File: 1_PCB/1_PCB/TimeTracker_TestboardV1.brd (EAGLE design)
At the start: 102.5 x 81.3 mm, 18 parts, among them IC1 7805DT, IC2 7805DT, J1 2908-05WB-MG, U1 WS2812B, U2 WS2812B, U3 WS2812B, U4 WS2812B

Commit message: fucvk u raj
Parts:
- added JP5: (no value), jumper:JP1
- added LED_12V1: (no value), led:SML0805
- added R3: 560, rcl:R0805
- added RESET1: (no value), switch-omron:B3F-10XX
- moved J1 4.02 mm to (7.62, 7.62)
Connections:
- new net GND1: RESET1.1, RESET1.2, U$1.RST
- new net N$12: JP5.2, U$1.RAW
- new net N$35: LED_12V1.A, R3.1
- net 5V: now also JP5.1
- net GND: now also LED_12V1.C, RESET1.3, RESET1.4, U$1.GND, U$1.GND1
- net N$1: now also R3.2
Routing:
- net N$13: track 0.00 -> 100.1 mm
- net N$12: track 0.00 -> 2.54 mm
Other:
- board size 102.5 x 81.3 mm -> 102.5 x 80 mm
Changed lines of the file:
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@@
 <board>
 <plain>
-<wire x1="-2.54" y1="-1.27" x2="100" y2="0" width="0" layer="20"/>
-<wire x1="100" y1="0" x2="100" y2="80" width="0" layer="20"/>
-<wire x1="100" y1="80" x2="-2.54" y2="78.73" width="0" layer="20"/>
+<wire x1="-2.54" y1="-1.27" x2="38.1" y2="-1.27" width="0" layer="20"/>
+<wire x1="38.1" y1="-1.27" x2="44.45" y2="5.08" width="0" layer="20"/>
+<wire x1="44.45" y1="5.08" x2="68.58" y2="5.08" width="0" layer="20"/>
+<wire x1="68.58" y1="5.08" x2="74.93" y2="-1.27" width="0" layer="20"/>
+<wire x1="74.93" y1="-1.27" x2="95.25" y2="-1.27" width="0" layer="20"/>
+<wire x1="95.25" y1="-1.27" x2="100" y2="2.635525" width="0" layer="20"/>
+<wire x1="100" y1="2.635525" x2="100" y2="76.19" width="0" layer="20"/>
+<wire x1="100" y1="76.19" x2="97.726525" y2="78.772415625" width="0" layer="20"/>
+<wire x1="97.726525" y1="78.772415625" x2="-2.54" y2="78.73" width="0" layer="20"/>
 <wire x1="-2.54" y1="78.73" x2="-2.54" y2="-1.27" width="0" layer="20"/>
 </plain>
@@
 </autorouter>
 <elements>
-<element name="J1" library="2908-05WB-MG" package="3M_2908-05WB-MG" value="2908-05WB-MG" x="11.43" y="8.89" smashed="yes" rot="R180">
-<attribute name="AVAILABILITY" value="Unavailable" x="-11.43" y="57.15" size="1.778" layer="27" rot="R180" display="off"/>
-<attribute name="DESCRIPTION" value=" 2908-05WB-MG Conn Micro S D Card HDR 8 POS 1.1mm So lder RA SMD T/R 0.5A RoHS " x="-11.43" y="57.15" size="1.778" layer="27" rot="R180" display="off"/>
-<attribute name="MF" value="3M" x="-11.43" y="57.15" size="1.778" layer="27" rot="R180" display="off"/>
-<attribute name="MP" value="2908-05WB-MG" x="-11.43" y="57.15" size="1.778" layer="27" rot="R180" display="off"/>
-<attribute name="NAME" x="19.07195" y="15.791759375" size="1.27031875" layer="25" rot="R270"/>
-<attribute name="PACKAGE" value="None" x="-11.43" y="57.15" size="1.778" layer="27" rot="R180" display="off"/>
-<attribute name="PRICE" value="None" x="-11.43" y="57.15" size="1.778" layer="27" rot="R180" display="off"/>
-<attribute name="VALUE" x="2.768609375" y="15.89111875" size="1.2702" layer="27" rot="R270"/>
+<element name="J1" library="2908-05WB-MG" package="3M_2908-05WB-MG" value="2908-05WB-MG" x="7.62" y="7.62" smashed="yes" rot="R180">
+<attribute name="AVAILABILITY" value="Unavailable" x="-15.24" y="55.88" size="1.778" layer="27" rot="R180" display="off"/>
+<attribute name="DESCRIPTION" value=" 2908-05WB-MG Conn Micro S D Card HDR 8 POS 1.1mm So lder RA SMD T/R 0.5A RoHS " x="-15.24" y="55.88" size="1.778" layer="27" rot="R180" display="off"/>
+<attribute name="MF" value="3M" x="-15.24" y="55.88" size="1.778" layer="27" rot="R180" display="off"/>
+<attribute name="MP" value="2908-05WB-MG" x="-15.24" y="55.88" size="1.778" layer="27" rot="R180" display="off"/>
+<attribute name="NAME" x="15.26195" y="14.521759375" size="1.27031875" layer="25" rot="R270"/>
+<attribute name="PACKAGE" value="None" x="-15.24" y="55.88" size="1.778" layer="27" rot="R180" display="off"/>
+<attribute name="PRICE" value="None" x="-15.24" y="55.88" size="1.778" layer="27" rot="R180" display="off"/>
+<attribute name="VALUE" x="-1.041390625" y="14.62111875" size="1.2702" layer="27" rot="R270"/>
 </element>
 <element name="U$1" library="NanoUSW" package="NANO" value="NANO" x="49.53" y="30.48" smashed="yes"/>
@@
 <attribute name="NAME" x="-11.43" y="-4.445" size="1.27" layer="25" ratio="10"/>
 <attribute name="VALUE" x="-11.43" y="-12.065" size="1.27" layer="27"/>
+</element>
+<element name="RESET1" library="switch-omron" library_urn="urn:adsk.eagle:library:377" package="B3F-10XX" package3d_urn="urn:adsk.eagle:package:27496/1" value="" x="31.369" y="24.384" smashed="yes">
+<attribute name="MF" value="" x="21.209" y="37.084" size="1.778" layer="27" display="off"/>
+<attribute name="MPN" value="B3F-1000" x="21.209" y="37.084" size="1.778" layer="27" display="off"/>
+<attribute name="NAME" x="28.321" y="28.067" size="1.27" layer="25" ratio="10"/>
+<attribute name="OC_FARNELL" value="176432" x="21.209" y="37.084" size="1.778" layer="27" display="off"/>
+<attribute name="OC_NEWARK" value="36M3542" x="21.209" y="37.084" size="1.778" layer="27" display="off"/>
+<attribute name="VALUE" x="28.321" y="19.304" size="1.27" layer="27" ratio="10"/>
+</element>
+<element name="R3" library="rcl" library_urn="urn:adsk.eagle:library:334" package="R0805" package3d_urn="urn:adsk.eagle:package:23553/2" value="560" x="1.27" y="66.04" smashed="yes" rot="R90">
+<attribute name="NAME" x="0" y="65.405" size="1.27" layer="25" rot="R90"/>
+<attribute name="SPICEPREFIX" value="R" x="1.27" y="66.04" size="1.778" layer="27" rot="R90" display="off"/>
+<attribute name="VALUE" x="3.81" y="65.405" size="1.27" layer="27" rot="R90"/>
+</element>
+<element name="LED_12V1" library="led" library_urn="urn:adsk.eagle:library:259" package="SML0805" package3d_urn="urn:adsk.eagle:package:15830/1" value="" x="1.27" y="60.96" smashed="yes" rot="R90">
+<attribute name="NAME" x="0.27" y="59.46" size="1.27" layer="25" rot="R90"/>
+<attribute name="VALUE" x="3.27" y="59.46" size="1.27" layer="27" rot="R90"/>
+</element>
+<element name="JP5" library="jumper" library_urn="urn:adsk.eagle:library:252" package="JP1" package3d_urn="urn:adsk.eagle:package:15455/1" value="" x="38.1" y="19.05" smashed="yes" rot="R270">
+<attribute name="NAME" x="35.56" y="20.701" size="1.27" layer="25" ratio="10"/>
+<attribute name="VALUE" x="35.56" y="16.129" size="1.27" layer="27" ratio="10"/>
 </element>
 </elements>
@@
 <wire x1="25.4" y1="64.45" x2="25.14" y2="67.59" width="0" layer="19" extent="1-1"/>
 <wire x1="23.7" y1="50.505" x2="25.4" y2="64.45" width="0" layer="19" extent="1-1"/>
-<wire x1="10.07" y1="5.59" x2="23.7" y2="50.505" width="0" layer="19" extent="1-1"/>
+<wire x1="6.26" y1="4.32" x2="23.7" y2="50.505" width="0" layer="19" extent="1-1"/>
 </signal>
 <signal name="GND">
@@
 <contactref element="U4" pad="3"/>
 <polygon width="0.1524" layer="1">
-<vertex x="-5.08" y="83.82"/>
-<vertex x="99.06" y="83.82"/>
+<vertex x="-2.54" y="86.36"/>
+<vertex x="96.52" y="86.36"/>
 <vertex x="107.95" y="74.93"/>
 <vertex x="107.95" y="-1.27"/>
 <vertex x="106.68" y="-2.54"/>
-<vertex x="-12.7" y="-2.54"/>
-<vertex x="-12.7" y="76.2"/>
+<vertex x="-15.24" y="-2.54"/>
+<vertex x="-15.24" y="73.66"/>
 </polygon>
+<contactref element="U$1" pad="GND"/>
+<contactref element="U$1" pad="GND1"/>
+<contactref element="RESET1" pad="3"/>
+<contactref element="RESET1" pad="4"/>
+<contactref element="LED_12V1" pad="C"/>
 </signal>
 <signal name="RFIDRESET">
@@
 <contactref element="J1" pad="7"/>
 <wire x1="54.61" y1="54.61" x2="85.09" y2="69.85" width="0" layer="19" extent="1-1"/>
-<wire x1="6.77" y1="5.79" x2="54.61" y2="54.61" width="0" layer="19" extent="1-1"/>
+<wire x1="2.96" y1="4.52" x2="54.61" y2="54.61" width="0" layer="19" extent="1-1"/>
 </signal>
 <signal name="SPISCK">
@@
 <contactref element="J1" pad="5"/>
 <wire x1="39.37" y1="57.15" x2="87.63" y2="69.85" width="0" layer="19" extent="1-1"/>
-<wire x1="8.97" y1="5.79" x2="39.37" y2="57.15" width="0" layer="19" extent="1-1"/>
+<wire x1="5.16" y1="4.52" x2="39.37" y2="57.15" width="0" layer="19" extent="1-1"/>
 </signal>
 <signal name="RFIDCS">
@@
 <wire x1="20.574" y1="65.339" x2="20.574" y2="67.584" width="0.6096" layer="1"/>
 <wire x1="20.574" y1="67.584" x2="20.58" y2="67.59" width="0.6096" layer="1"/>
+<contactref element="R3" pad="2"/>
+<wire x1="1.27" y1="66.99" x2="12.446" y2="65.217" width="0" layer="19" extent="1-1"/>
 </signal>
 <signal name="5V">
@@
 <wire x1="33.401" y1="10.668" x2="38.975" y2="10.668" width="0.2032" layer="1"/>
 <wire x1="38.975" y1="10.668" x2="40.677" y2="12.37" width="0.2032" layer="1"/>
+<contactref element="JP5" pad="1"/>
 <wire x1="7.88" y1="63.22" x2="7.62" y2="65.09" width="0" layer="19" extent="1-1"/>
-<wire x1="31.787" y1="12.37" x2="7.88" y2="63.22" width="0" layer="19" extent="1-1"/>
+<wire x1="36.83" y1="19.05" x2="7.88" y2="63.22" width="0" layer="19" extent="1-1"/>
+<wire x1="40.677" y1="12.37" x2="36.83" y2="19.05" width="0" layer="19" extent="1-1"/>
 </signal>
 <signal name="N$9">
@@
 <wire x1="34.987" y1="12.37" x2="35.523" y2="12.37" width="0.1524" layer="1"/>
 </signal>
+<signal name="GND1">
+<contactref element="RESET1" pad="1"/>
+<contactref element="RESET1" pad="2"/>
+<contactref element="U$1" pad="RST"/>
+<wire x1="34.6202" y1="26.6446" x2="39.37" y2="26.67" width="0" layer="19" extent="1-1"/>
+<wire x1="28.1178" y1="26.6446" x2="34.6202" y2="26.6446" width="0" layer="19" extent="1-1"/>
+</signal>
+<signal name="N$35">
+<contactref element="R3" pad="1"/>
+<contactref element="LED_12V1" pad="A"/>
+<wire x1="1.27" y1="62.01" x2="1.27" y2="65.09" width="0" layer="19" extent="1-1"/>
+</signal>
+<signal name="N$12">
+<contactref element="JP5" pad="2"/>
+<contactref element="U$1" pad="RAW"/>
+<wire x1="39.37" y1="19.05" x2="39.37" y2="21.59" width="0.3048" layer="16"/>
+</signal>
+<signal name="N$13">
+<wire x1="41.021" y1="58.42" x2="52.959" y2="58.42" width="0.1524" layer="1"/>
+<wire x1="52.959" y1="58.42" x2="52.959" y2="20.32" width="0.1524" layer="1"/>
+<wire x1="52.959" y1="20.32" x2="41.021" y2="20.32" width="0.1524" layer="1"/>
+<wire x1="41.021" y1="20.32" x2="41.021" y2="58.42" width="0.1524" layer="1"/>
+</signal>
 </signals>

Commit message: First Commit Mitun
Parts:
- moved J1 26.7 mm to (7.62, 34.3), turned to 270 degrees
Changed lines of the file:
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@@
 <?xml version="1.0" encoding="utf-8"?>
 <!DOCTYPE eagle SYSTEM "eagle.dtd">
-<eagle version="9.3.0">
+<eagle version="9.2.2">
 <drawing>
 <settings>
@@
 </autorouter>
 <elements>
-<element name="J1" library="2908-05WB-MG" package="3M_2908-05WB-MG" value="2908-05WB-MG" x="7.62" y="7.62" smashed="yes" rot="R180">
-<attribute name="AVAILABILITY" value="Unavailable" x="-15.24" y="55.88" size="1.778" layer="27" rot="R180" display="off"/>
-<attribute name="DESCRIPTION" value=" 2908-05WB-MG Conn Micro S D Card HDR 8 POS 1.1mm So lder RA SMD T/R 0.5A RoHS " x="-15.24" y="55.88" size="1.778" layer="27" rot="R180" display="off"/>
-<attribute name="MF" value="3M" x="-15.24" y="55.88" size="1.778" layer="27" rot="R180" display="off"/>
-<attribute name="MP" value="2908-05WB-MG" x="-15.24" y="55.88" size="1.778" layer="27" rot="R180" display="off"/>
-<attribute name="NAME" x="15.26195" y="14.521759375" size="1.27031875" layer="25" rot="R270"/>
-<attribute name="PACKAGE" value="None" x="-15.24" y="55.88" size="1.778" layer="27" rot="R180" display="off"/>
-<attribute name="PRICE" value="None" x="-15.24" y="55.88" size="1.778" layer="27" rot="R180" display="off"/>
-<attribute name="VALUE" x="-1.041390625" y="14.62111875" size="1.2702" layer="27" rot="R270"/>
+<element name="J1" library="2908-05WB-MG" package="3M_2908-05WB-MG" value="2908-05WB-MG" x="7.62" y="34.29" smashed="yes" rot="R270">
+<attribute name="AVAILABILITY" value="Unavailable" x="-40.64" y="11.43" size="1.778" layer="27" rot="R270" display="off"/>
+<attribute name="DESCRIPTION" value=" 2908-05WB-MG Conn Micro S D Card HDR 8 POS 1.1mm So lder RA SMD T/R 0.5A RoHS " x="-40.64" y="11.43" size="1.778" layer="27" rot="R270" display="off"/>
+<attribute name="MF" value="3M" x="-40.64" y="11.43" size="1.778" layer="27" rot="R270" display="off"/>
+<attribute name="MP" value="2908-05WB-MG" x="-40.64" y="11.43" size="1.778" layer="27" rot="R270" display="off"/>
+<attribute name="NAME" x="0.718240625" y="41.93195" size="1.27031875" layer="25"/>
+<attribute name="PACKAGE" value="None" x="-40.64" y="11.43" size="1.778" layer="27" rot="R270" display="off"/>
+<attribute name="PRICE" value="None" x="-40.64" y="11.43" size="1.778" layer="27" rot="R270" display="off"/>
+<attribute name="VALUE" x="0.61888125" y="25.628609375" size="1.2702" layer="27"/>
 </element>
 <element name="U$1" library="NanoUSW" package="NANO" value="NANO" x="49.53" y="30.48" smashed="yes"/>
@@
 <wire x1="25.4" y1="64.45" x2="25.14" y2="67.59" width="0" layer="19" extent="1-1"/>
 <wire x1="23.7" y1="50.505" x2="25.4" y2="64.45" width="0" layer="19" extent="1-1"/>
-<wire x1="6.26" y1="4.32" x2="23.7" y2="50.505" width="0" layer="19" extent="1-1"/>
+<wire x1="10.92" y1="32.93" x2="23.7" y2="50.505" width="0" layer="19" extent="1-1"/>
 </signal>
 <signal name="GND">
@@
 <contactref element="J1" pad="7"/>
 <wire x1="54.61" y1="54.61" x2="85.09" y2="69.85" width="0" layer="19" extent="1-1"/>
-<wire x1="2.96" y1="4.52" x2="54.61" y2="54.61" width="0" layer="19" extent="1-1"/>
+<wire x1="10.72" y1="29.63" x2="54.61" y2="54.61" width="0" layer="19" extent="1-1"/>
 </signal>
 <signal name="SPISCK">
@@
 <contactref element="J1" pad="5"/>
 <wire x1="39.37" y1="57.15" x2="87.63" y2="69.85" width="0" layer="19" extent="1-1"/>
-<wire x1="5.16" y1="4.52" x2="39.37" y2="57.15" width="0" layer="19" extent="1-1"/>
+<wire x1="10.72" y1="31.83" x2="39.37" y2="57.15" width="0" layer="19" extent="1-1"/>
 </signal>
 <signal name="RFIDCS">

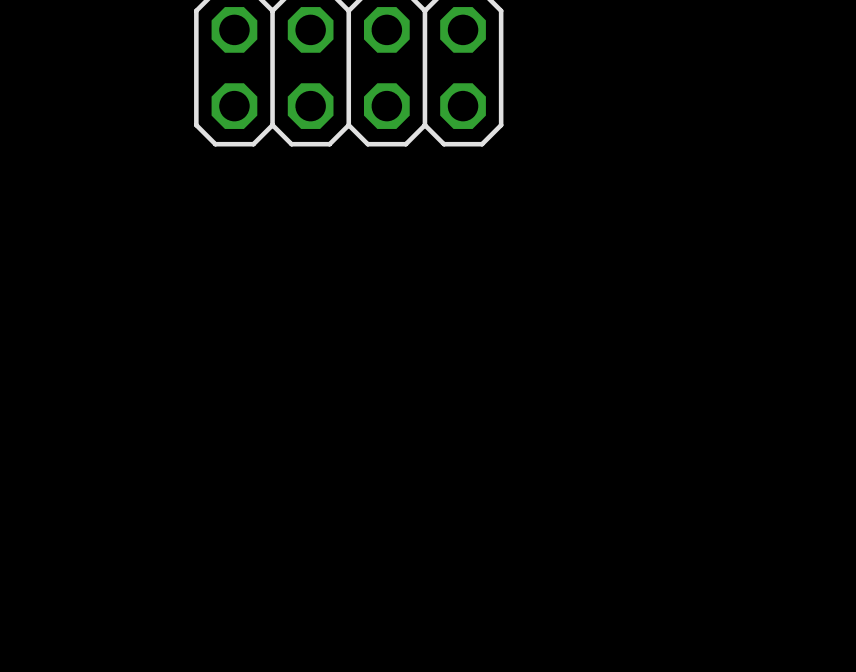
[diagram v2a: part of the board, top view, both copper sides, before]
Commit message: Battery Holder and Oscillator Added to circtuit
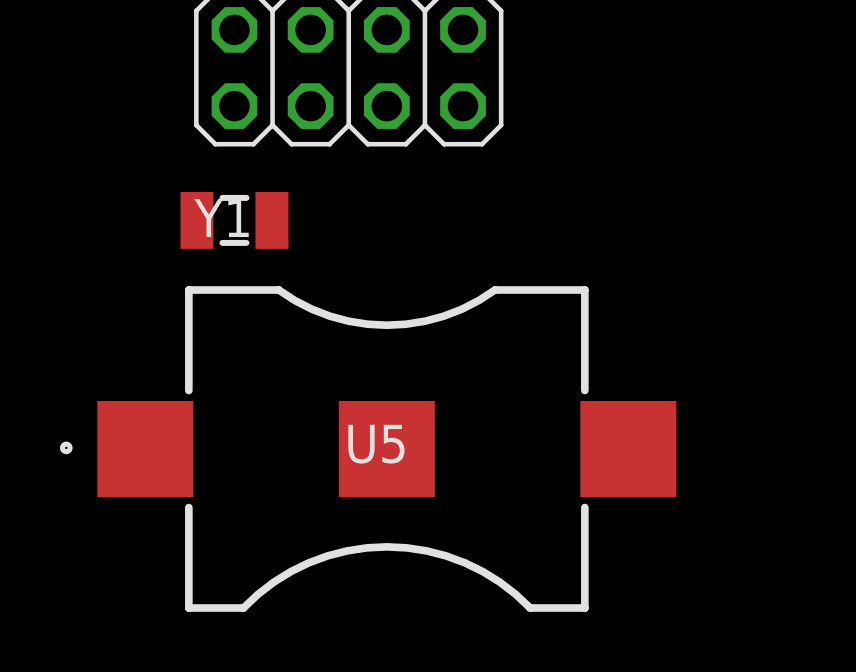
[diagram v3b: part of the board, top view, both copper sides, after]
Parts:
- added U5: SMTM1225, SamacSys_Parts:SMTM1225
- added Y1: FX135A-327, SamacSys_Parts:FX135
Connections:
- new net N$14: U$2.1, Y1.2
- new net N$15: U$2.2, Y1.1
- new net N$16: U$2.3, U5.1
- net GND: now also U5.2
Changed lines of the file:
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@@
 <attribute name="VALUE" x="35.56" y="16.129" size="1.27" layer="27" ratio="10"/>
+</element>
+<element name="Y1" library="SamacSys_Parts" package="FX135" value="FX135A-327" x="-10.16" y="-12.7" smashed="yes">
+<attribute name="DESCRIPTION" value="Crystal SMD 32.768kHz 1.5x3.2mm Crystal 32.768kHz, +/-20ppm, 2-Pin SMD, 3.2 x 1.5 x 0.9mm" x="-10.16" y="-12.7" size="1.778" layer="27" display="off"/>
+<attribute name="HEIGHT" value="mm" x="-10.16" y="-12.7" size="1.778" layer="27" display="off"/>
+<attribute name="MANUFACTURER_NAME" value="Fox" x="-10.16" y="-12.7" size="1.778" layer="27" display="off"/>
+<attribute name="MANUFACTURER_PART_NUMBER" value="FX135A-327" x="-10.16" y="-12.7" size="1.778" layer="27" display="off"/>
+<attribute name="MOUSER_PART_NUMBER" value="559-FX135A-327" x="-10.16" y="-12.7" size="1.778" layer="27" display="off"/>
+<attribute name="MOUSER_PRICE-STOCK" value="https://www.mouser.com/Search/Refine.aspx?Keyword=559-FX135A-327" x="-10.16" y="-12.7" size="1.778" layer="27" display="off"/>
+<attribute name="NAME" x="-10.517" y="-12.62" size="1.27" layer="25" align="center"/>
+<attribute name="RS_PART_NUMBER" value="6480200P" x="-10.16" y="-12.7" size="1.778" layer="27" display="off"/>
+<attribute name="RS_PRICE-STOCK" value="http://uk.rs-online.com/web/p/products/6480200P" x="-10.16" y="-12.7" size="1.778" layer="27" display="off"/>
+<attribute name="VALUE" x="-10.517" y="-12.62" size="1.27" layer="27" align="center"/>
+</element>
+<element name="U5" library="SamacSys_Parts" package="SMTM1225" value="SMTM1225" x="-5.08" y="-20.32" smashed="yes">
+<attribute name="DESCRIPTION" value="Coin Cell Battery Holders SMT HOLDER FOR CR1225" x="-5.08" y="-20.32" size="1.778" layer="27" display="off"/>
+<attribute name="HEIGHT" value="mm" x="-5.08" y="-20.32" size="1.778" layer="27" display="off"/>
+<attribute name="MANUFACTURER_NAME" value="RENATA" x="-5.08" y="-20.32" size="1.778" layer="27" display="off"/>
+<attribute name="MANUFACTURER_PART_NUMBER" value="SMTM1225" x="-5.08" y="-20.32" size="1.778" layer="27" display="off"/>
+<attribute name="MOUSER_PART_NUMBER" value="614-SMTM1225" x="-5.08" y="-20.32" size="1.778" layer="27" display="off"/>
+<attribute name="MOUSER_PRICE-STOCK" value="https://www.mouser.com/Search/Refine.aspx?Keyword=614-SMTM1225" x="-5.08" y="-20.32" size="1.778" layer="27" display="off"/>
+<attribute name="NAME" x="-5.426" y="-20.147" size="1.27" layer="25" align="center"/>
+<attribute name="RS_PART_NUMBER" value="" x="-5.08" y="-20.32" size="1.778" layer="27" display="off"/>
+<attribute name="RS_PRICE-STOCK" value="" x="-5.08" y="-20.32" size="1.778" layer="27" display="off"/>
+<attribute name="VALUE" x="-5.426" y="-20.147" size="1.27" layer="27" align="center"/>
 </element>
 </elements>
@@
 <contactref element="RESET1" pad="4"/>
 <contactref element="LED_12V1" pad="C"/>
+<contactref element="U5" pad="2"/>
+<wire x1="54.61" y1="29.21" x2="77.47" y2="69.85" width="0" layer="19" extent="1-1"/>
+<wire x1="39.37" y1="24.13" x2="54.61" y2="29.21" width="0" layer="19" extent="1-1"/>
+<wire x1="34.6202" y1="22.1234" x2="39.37" y2="24.13" width="0" layer="19" extent="1-1"/>
+<wire x1="28.1178" y1="22.1234" x2="34.6202" y2="22.1234" width="0" layer="19" extent="1-1"/>
+<wire x1="35.523" y1="15.57" x2="34.6202" y2="22.1234" width="0" layer="19" extent="1-1"/>
+<wire x1="35.523" y1="9.22" x2="35.523" y2="15.57" width="0" layer="19" extent="1-1"/>
+<wire x1="26.633" y1="15.57" x2="28.1178" y2="22.1234" width="0" layer="19" extent="1-1"/>
+<wire x1="26.633" y1="9.22" x2="26.633" y2="15.57" width="0" layer="19" extent="1-1"/>
+<wire x1="10.92" y1="30.73" x2="28.1178" y2="22.1234" width="0" layer="19" extent="1-1"/>
+<wire x1="19.48" y1="48.555" x2="10.92" y2="30.73" width="0" layer="19" extent="1-1"/>
+<wire x1="10.16" y1="55.92" x2="19.48" y2="48.555" width="0" layer="19" extent="1-1"/>
+<wire x1="1.27" y1="59.91" x2="10.16" y2="55.92" width="0" layer="19" extent="1-1"/>
+<wire x1="7.62" y1="66.99" x2="1.27" y2="59.91" width="0" layer="19" extent="1-1"/>
+<wire x1="12.446" y1="67.117" x2="7.62" y2="66.99" width="0" layer="19" extent="1-1"/>
+<wire x1="5.89" y1="74.93" x2="7.62" y2="66.99" width="0" layer="19" extent="1-1"/>
+<wire x1="20.574" y1="63.439" x2="12.446" y2="67.117" width="0" layer="19" extent="1-1"/>
+<wire x1="25.4" y1="62.55" x2="20.574" y2="63.439" width="0" layer="19" extent="1-1"/>
+<wire x1="22.86" y1="74.89" x2="20.574" y2="63.439" width="0" layer="19" extent="1-1"/>
+<wire x1="-5.08" y1="-20.32" x2="26.633" y2="9.22" width="0" layer="19" extent="1-1"/>
 </signal>
 <signal name="RFIDRESET">
@@
 <wire x1="41.021" y1="20.32" x2="41.021" y2="58.42" width="0.1524" layer="1"/>
 </signal>
+<signal name="N$14">
+<contactref element="Y1" pad="2"/>
+<contactref element="U$2" pad="1"/>
+<wire x1="-8.91" y1="-12.7" x2="19.48" y2="50.505" width="0" layer="19" extent="1-1"/>
+</signal>
+<signal name="N$15">
+<contactref element="Y1" pad="1"/>
+<contactref element="U$2" pad="2"/>
+<wire x1="-11.41" y1="-12.7" x2="19.48" y2="49.855" width="0" layer="19" extent="1-1"/>
+</signal>
+<signal name="N$16">
+<contactref element="U5" pad="1"/>
+<contactref element="U$2" pad="3"/>
+<wire x1="-13.13" y1="-20.32" x2="19.48" y2="49.205" width="0" layer="19" extent="1-1"/>
+</signal>
 </signals>
